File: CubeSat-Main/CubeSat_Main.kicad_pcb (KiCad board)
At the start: 2 copper layers, 92 x 92 mm, 25 parts, among them J1 Conn_01x03_Pin, J2 Conn_01x08_Socket, U1 STM32F411CEU6 - BlackPill, U2 LORA E220-900T22D, U3 BNO055, U4 GPS_NEO6M, U6 LM35-LP

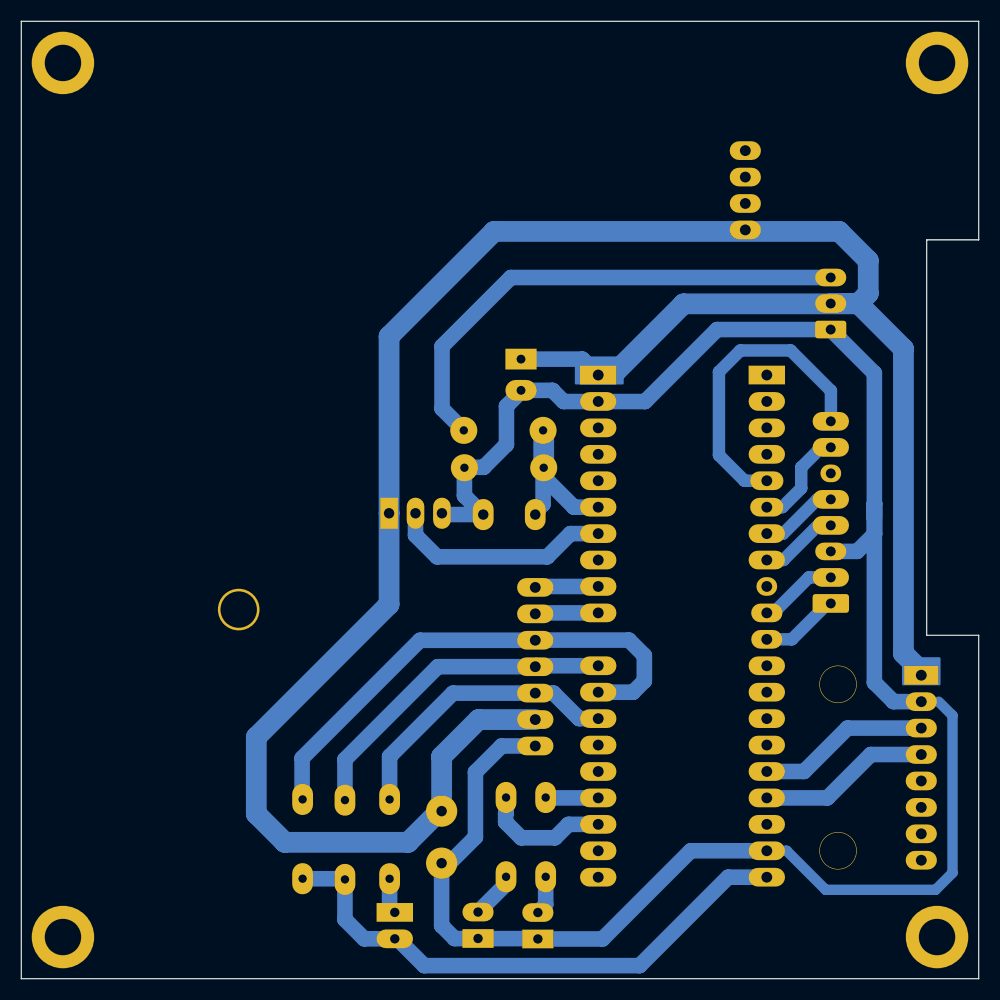
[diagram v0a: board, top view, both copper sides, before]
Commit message: adding the unused pin as smd, instead of just removing it
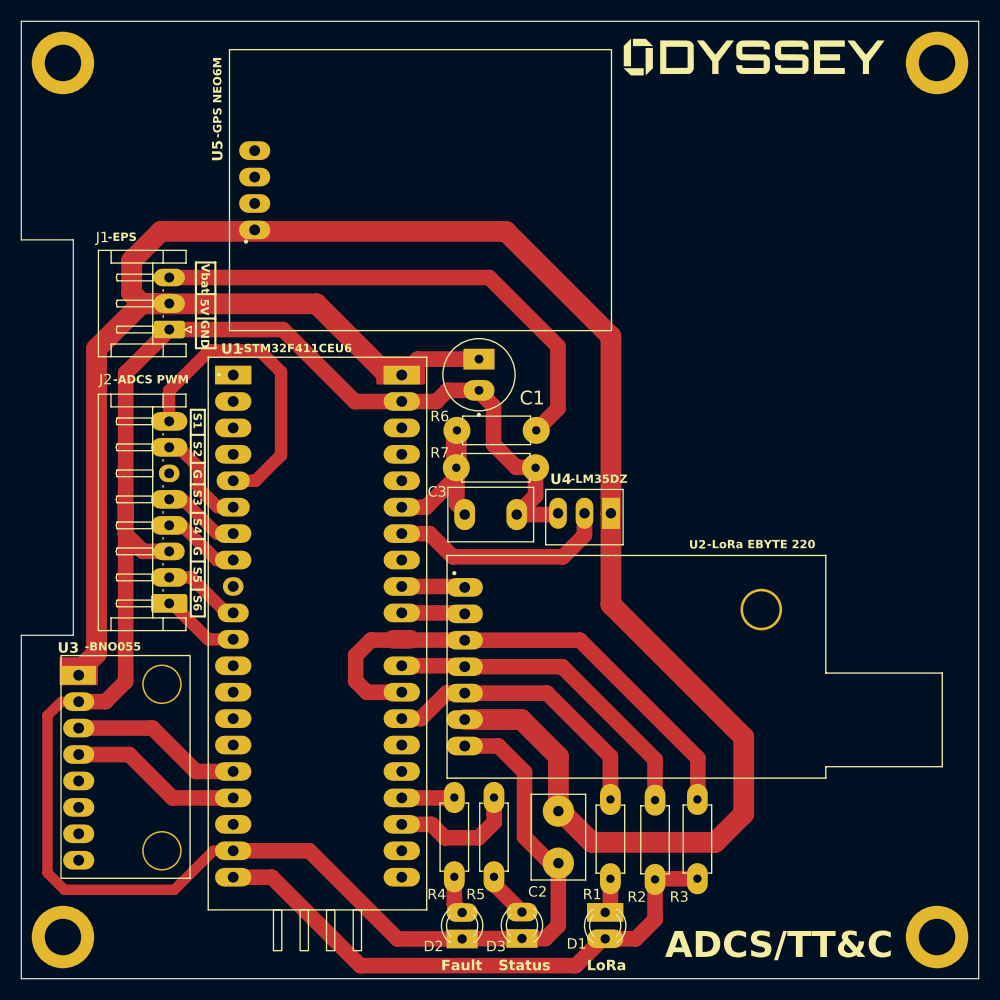
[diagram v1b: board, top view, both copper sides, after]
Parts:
- C1, C2, C3, D1, D2, D3, G***, J1, J2, R1, R2, R3, R4, R5, R6, R7, REF** (x4), U1, U2, U3: moved to F.Cu
- U4: renamed from U6; moved to F.Cu
- U5: renamed from U4; moved to F.Cu
- moved REF** 84.0 mm to (88.0, -4.00), turned to 0 degrees
- moved REF** 84.0 mm to (4.00, -4.00), turned to 0 degrees
- moved REF** 84.0 mm to (88.0, -88.0), turned to 0 degrees
- moved REF** 84.0 mm to (4.00, -88.0), turned to 0 degrees
- moved U3 72.0 mm to (10.0, -20.3), turned to 180 degrees
- moved J2 63.6 mm to (14.2, -36.1)
- moved J1 63.6 mm to (14.2, -62.4)
- moved G*** 49.0 mm to (70.5, -88.6), turned to 0 degrees
- moved R3 37.9 mm to (65.0, -17.2)
- moved U1 35.1 mm to (28.5, -33.5), turned to 0 degrees
- moved R2 29.8 mm to (60.9, -17.2)
- moved U2 26.2 mm to (59.1, -30.0)
- moved R1 21.2 mm to (56.6, -17.2)
- moved D1 20.2 mm to (56.1, -6.37)
- moved U4 16.2 mm to (54.1, -44.7)
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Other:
- outline, holes or cut-outs redrawn

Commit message: change in the GPS location, so it doesnt smash into its antenna
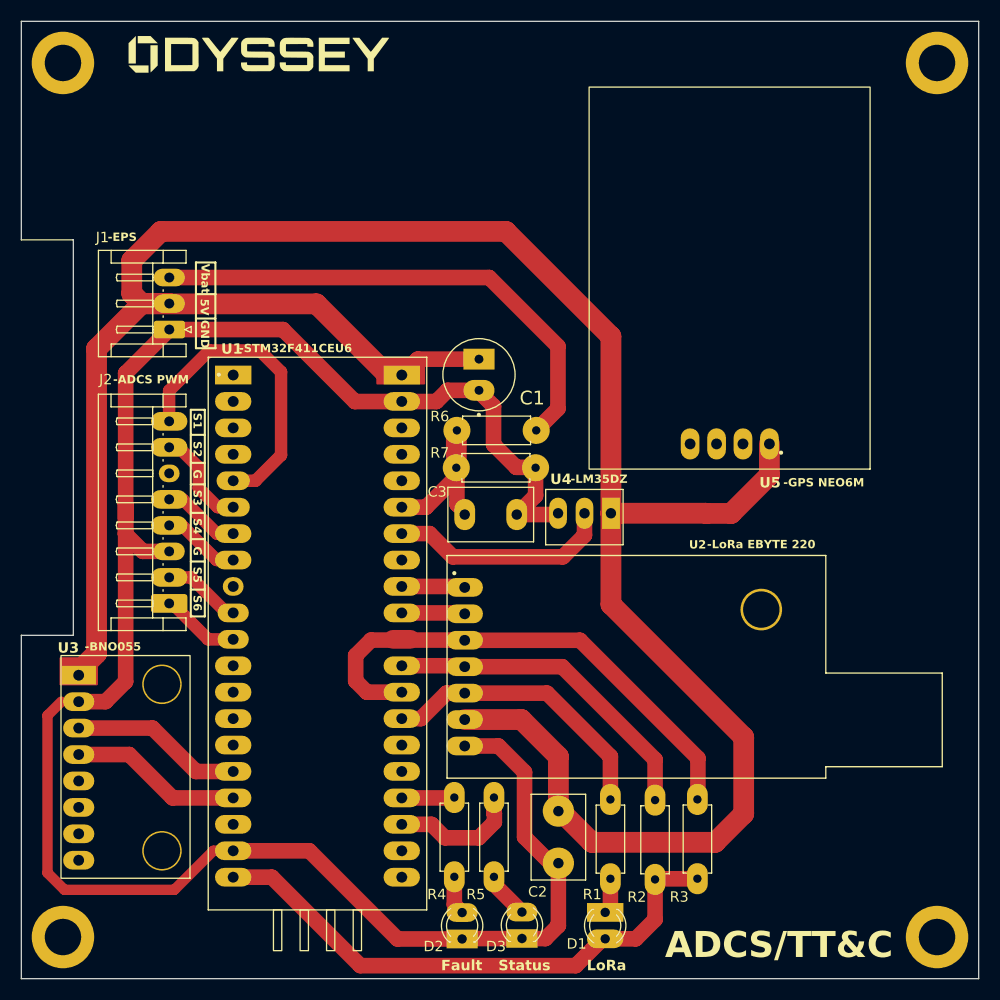
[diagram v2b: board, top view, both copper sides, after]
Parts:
- moved G*** 47.6 mm to (22.9, -88.8)
- moved U5 31.4 mm to (68.0, -66.9), turned to 180 degrees
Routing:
- net VIN_5V: track 219.1 -> 238.9 mm
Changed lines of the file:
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@@
 	(footprint "Cubesat_Modules:GPS_NEO6M"
 		(layer "F.Cu")
-		(at 37.915 -75.895 90)
+		(at 67.95 -66.88 180)
 		(property "Reference" "U5"
-			(at 3.665 -19.055 90)
+			(at -4 -19.21 0)
 			(unlocked yes)
 			(layer "F.SilkS")
@@
 		)
 		(property "Value" "GPS_NEO6M"
-			(at 0 -1.5 90)
+			(at 0 -1.5 180)
 			(unlocked yes)
 			(layer "F.Fab")
@@
 		)
 		(property "Datasheet" ""
-			(at 0 0 90)
+			(at 0 0 180)
 			(unlocked yes)
 			(layer "F.Fab")
@@
 		)
 		(property "Description" ""
-			(at 0 0 90)
+			(at 0 0 180)
 			(unlocked yes)
 			(layer "F.Fab")
@@
 		)
 		(fp_text user "${REFERENCE}"
-			(at 0 0 90)
+			(at 0 0 180)
 			(unlocked yes)
 			(layer "F.Fab")
@@
 		)
 		(pad "1" thru_hole oval
-			(at -3.94 -15.49 180)
+			(at -3.94 -15.49 270)
 			(size 3 1.8)
 			(drill 1.04)
@@
 		)
 		(pad "2" thru_hole oval
-			(at -1.4 -15.49 180)
+			(at -1.4 -15.49 270)
 			(size 3 1.8)
 			(drill 1.04)
@@
 		)
 		(pad "3" thru_hole oval
-			(at 1.14 -15.49 180)
+			(at 1.14 -15.49 270)
 			(size 3 1.8)
 			(drill 1.04)
@@
 		)
 		(pad "4" thru_hole oval
-			(at 3.68 -15.49 180)
+			(at 3.68 -15.49 270)
 			(size 3 1.8)
 			(drill 1.04)
@@
 		)
 		(property "Value" "Conn_01x03_Pin"
-			(at 19.3375 -0.350002 90)
+			(at 11.49 -1.66 0)
 			(layer "F.Fab")
 			(effects
@@
 	(footprint "Logos:Odyssey_Logo_2"
 		(layer "F.Cu")
-		(at 70.49 -88.56)
+		(at 22.901622 -88.824623)
 		(property "Reference" "G***"
 			(at 4.318378 10.074623 0)
@@
 	)
 	(gr_text "-GPS NEO6M"
-		(at 19.32 -80.79 90)
+		(at 73.22 -47.21 0)
 		(layer "F.SilkS")
 		(effects
@@
 	)
 	(segment
+		(start 65.805 -44.725)
+		(end 65.82 -44.71)
+		(width 2)
+		(layer "F.Cu")
+		(net 1)
+	)
+	(segment
 		(start 46.57 -71.81)
 		(end 13.41 -71.81)
@@
 	)
 	(segment
+		(start 68.22 -44.71)
+		(end 71.89 -48.38)
+		(width 2)
+		(layer "F.Cu")
+		(net 1)
+	)
+	(segment
 		(start 51.61 -21.35)
 		(end 48.06 -24.9)
@@
 	)
 	(segment
+		(start 65.82 -44.71)
+		(end 68.22 -44.71)
+		(width 2)
+		(layer "F.Cu")
+		(net 1)
+	)
+	(segment
 		(start 34.9225 -58.2875)
 		(end 36.46 -58.2875)
@@
 		(width 2)
 		(layer "F.Cu")
+		(net 1)
+	)
+	(segment
+		(start 71.89 -48.38)
+		(end 71.89 -51.39)
+		(width 2)
+		(layer "F.Cu")
+		(net 1)
+	)
+	(segment
+		(start 56.66 -44.725)
+		(end 65.805 -44.725)
+		(width 2)
+		(layer "F.Cu")

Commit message: small changes only
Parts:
- C1, C2, C3, D1, D2, D3, G***, J1, J2, R1, R2, R3, R4, R5, R6, R7, REF** (x4), U1, U2, U3, U4, U5: moved to B.Cu
- moved REF** 84.0 mm to (4.00, -4.00), turned to 180 degrees
- moved REF** 84.0 mm to (88.0, -4.00), turned to 180 degrees
- moved REF** 84.0 mm to (4.00, -88.0), turned to 180 degrees
- moved REF** 84.0 mm to (88.0, -88.0), turned to 180 degrees
- moved U3 72.0 mm to (82.0, -20.3), turned to 0 degrees
- moved J2 63.6 mm to (77.8, -36.1)
- moved J1 63.6 mm to (77.8, -62.4)
- moved G*** 46.2 mm to (69.1, -88.8), turned to 180 degrees
- moved U5 43.9 mm to (24.1, -66.9), turned to 0 degrees
- moved R3 37.9 mm to (27.0, -17.2)
- moved U1 35.1 mm to (63.5, -33.5), turned to 180 degrees
- moved R2 29.8 mm to (31.1, -17.2)
- moved U2 26.2 mm to (32.9, -30.0)
- moved R1 21.2 mm to (35.4, -17.2)
- moved D1 20.2 mm to (35.9, -6.37)
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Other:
- outline, holes or cut-outs redrawn

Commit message: small changes in layout
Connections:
- U1 pad 26: unconnected-(U1-PB13-Pad26) -> M1_PWM1
- U1 pad 27: unconnected-(U1-PB14-Pad27) -> M1_PWM2
- U1 pad 29: M1_PWM1 -> unconnected-(U1-PA8-Pad29)
- U1 pad 30: M1_PWM2 -> unconnected-(U1-PA9-Pad30)
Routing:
- net M1_PWM1: track 30.4 -> 7.00 mm
- net M1_PWM2: track 9.70 -> 6.92 mm
- net unconnected-(U1-PA8-Pad29): track 0.00 -> 0.51 mm
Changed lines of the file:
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@@
 	(net 41 "unconnected-(U1-5V-Pad5V2)")
 	(net 42 "unconnected-(U3-ADO-Pad5)")
-	(net 43 "unconnected-(U1-PB14-Pad27)")
-	(net 44 "unconnected-(U1-PB13-Pad26)")
+	(net 43 "unconnected-(U1-PA9-Pad30)")
+	(net 44 "unconnected-(U1-PA8-Pad29)")
 	(net 45 "unconnected-(U5-TX-Pad3)")
 	(net 46 "unconnected-(U5-GND-Pad4)")
@@
 			(layers "*.Cu" "*.Mask")
 			(remove_unused_layers no)
-			(net 44 "unconnected-(U1-PB13-Pad26)")
+			(net 4 "M1_PWM1")
 			(pinfunction "PB13")
-			(pintype "bidirectional+no_connect")
+			(pintype "bidirectional")
 			(solder_mask_margin 0.102)
 		)
@@
 			(layers "*.Cu" "*.Mask")
 			(remove_unused_layers no)
-			(net 43 "unconnected-(U1-PB14-Pad27)")
+			(net 17 "M1_PWM2")
 			(pinfunction "PB14")
-			(pintype "bidirectional+no_connect")
+			(pintype "bidirectional")
 			(solder_mask_margin 0.102)
 		)
@@
 			(layers "*.Cu" "*.Mask")
 			(remove_unused_layers no)
-			(net 4 "M1_PWM1")
+			(net 44 "unconnected-(U1-PA8-Pad29)")
 			(pinfunction "PA8")
-			(pintype "bidirectional")
+			(pintype "bidirectional+no_connect")
 			(solder_mask_margin 0.102)
 		)
@@
 			(layers "*.Cu" "*.Mask")
 			(remove_unused_layers no)
-			(net 17 "M1_PWM2")
+			(net 43 "unconnected-(U1-PA9-Pad30)")
 			(pinfunction "PA9")
-			(pintype "bidirectional")
+			(pintype "bidirectional+no_connect")
 			(solder_mask_margin 0.102)
 		)
@@
 		(pad "33" thru_hole oval
 			(at -8.1 4.18 180)
-			(size 2 1.8)
+			(size 1.8 1.8)
 			(drill 1.04)
 			(layers "*.Cu" "*.Mask")
@@
 		(pad "6" thru_hole oval
 			(at 12.5 0 90)
-			(size 1.7 2)
+			(size 1.8 3.5)
 			(drill 0.95)
 			(layers "*.Cu" "*.Mask")
@@
 	)
 	(gr_rect
-		(start 75.715 -54.67)
-		(end 74.365 -34.81)
+		(start 74.365 -54.67)
+		(end 75.715 -34.81)
 		(stroke
 			(width 0.2)
@@
 	)
 	(gr_rect
-		(start 75.22 -68.825)
-		(end 73.35 -60.585)
+		(start 73.35 -68.825)
+		(end 75.22 -60.585)
 		(stroke
 			(width 0.2)
@@
 	)
 	(segment
-		(start 67.04 -50.31)
-		(end 69.5 -47.85)
-		(width 1.2)
-		(layer "B.Cu")
-		(net 4)
-	)
-	(segment
-		(start 77.8 -56.5)
-		(end 73.93 -60.37)
-		(width 1.2)
-		(layer "B.Cu")
-		(net 4)
-	)
-	(segment
-		(start 67.04 -58.31)
-		(end 67.04 -50.31)
-		(width 1.2)
-		(layer "B.Cu")
-		(net 4)
-	)
-	(segment
-		(start 69.5 -47.85)
-		(end 71.64 -47.85)
-		(width 1.2)
-		(layer "B.Cu")
-		(net 4)
-	)
-	(segment
-		(start 77.79 -53.56)
-		(end 77.8 -53.57)
-		(width 1.2)
-		(layer "B.Cu")
-		(net 4)
-	)
-	(segment
-		(start 71.64 -47.949939)
-		(end 71.64 -47.95)
-		(width 0.2)
-		(layer "B.Cu")
-		(net 4)
-	)
-	(segment
-		(start 71.6575 -47.932439)
-		(end 71.64 -47.949939)
-		(width 0.2)
+		(start 75.88 -55.47)
+		(end 71.64 -55.47)
+		(width 1.5)
 		(layer "B.Cu")
 		(net 4)
@@
 	)
 	(segment
-		(start 77.8 -53.57)
-		(end 77.8 -56.5)
-		(width 1.2)
-		(layer "B.Cu")
-		(net 4)
-	)
-	(segment
-		(start 69.1 -60.37)
-		(end 67.04 -58.31)
-		(width 1.2)
-		(layer "B.Cu")
-		(net 4)
-	)
-	(segment
-		(start 71.64 -47.85)
-		(end 72.13 -47.85)
-		(width 1)
+		(start 77.79 -53.56)
+		(end 75.88 -55.47)
+		(width 1.5)
 		(layer "B.Cu")
 		(net 4)
 	)
 	(segment
-		(start 73.93 -60.37)
-		(end 69.1 -60.37)
+		(start 76.25 -46.06)
+		(end 77.79 -46.06)
 		(width 1.2)
 		(layer "B.Cu")
-		(net 4)
+		(net 7)
 	)
 	(segment
@@
 	)
 	(segment
-		(start 76.5 -46.06)
-		(end 77.79 -46.06)
+		(start 71.64 -42.77)
+		(end 72.96 -42.77)
 		(width 1.2)
 		(layer "B.Cu")
@@
 	)
 	(segment
-		(start 71.707561 -42.83)
-		(end 71.73 -42.852439)
-		(width 0.2)
-		(layer "B.Cu")
-		(net 7)
-	)
-	(segment
-		(start 71.64 -42.77)
-		(end 73.21 -42.77)
+		(start 72.96 -42.77)
+		(end 76.25 -46.06)
 		(width 1.2)
 		(layer "B.Cu")
@@
 	)
 	(segment
-		(start 73.21 -42.77)
-		(end 76.5 -46.06)
-		(width 1.2)
+		(start 71.707561 -42.83)
+		(end 71.73 -42.852439)
+		(width 0.2)
 		(layer "B.Cu")
 		(net 7)
@@
 		(start 74.05 -32.61)
 		(end 71.64 -32.61)
-		(width 1.2)
+		(width 1.5)
 		(layer "B.Cu")
 		(net 12)
@@
 		(start 77.79 -36.06)
 		(end 77.5 -36.06)
-		(width 1.2)
+		(width 1.5)
 		(layer "B.Cu")
 		(net 12)
@@
 		(start 77.5 -36.06)
 		(end 74.05 -32.61)
-		(width 1.2)
+		(width 1.5)
 		(layer "B.Cu")
 		(net 12)
@@
 	)
 	(segment
-		(start 72.27 -35.15)
+		(start 72.37 -35.15)
 		(end 71.64 -35.15)
-		(width 1.2)
+		(width 1.5)
 		(layer "B.Cu")
 		(net 16)
 	)
 	(segment
-		(start 75.68 -38.56)
-		(end 72.27 -35.15)
-		(width 1.2)
+		(start 75.78 -38.56)
+		(end 72.37 -35.15)
+		(width 1.5)
 		(layer "B.Cu")
 		(net 16)
@@
 	(segment
 		(start 77.79 -38.56)
-		(end 75.68 -38.56)
-		(width 1.2)
+		(end 75.78 -38.56)
+		(width 1.5)
 		(layer "B.Cu")
 		(net 16)
 	)
 	(segment
-		(start 74.95 -49.13)
-		(end 76.88 -51.06)
-		(width 1.2)
+		(start 73.44 -52.93)
+		(end 75.31 -51.06)
+		(width 1.5)
 		(layer "B.Cu")
 		(net 17)
 	)
 	(segment
-		(start 76.88 -51.06)
+		(start 75.31 -51.06)
 		(end 77.79 -51.06)
-		(width 1.2)
-		(layer "B.Cu")
-		(net 17)
-	)
-	(segment
-		(start 74.95 -47.13)
-		(end 74.95 -49.13)
-		(width 1.2)
-		(layer "B.Cu")
-		(net 17)
-	)
-	(segment
-		(start 73.13 -45.31)
-		(end 74.95 -47.13)
-		(width 1.2)
+		(width 1.5)
 		(layer "B.Cu")
 		(net 17)
 	)
 	(segment
-		(start 71.64 -45.31)
-		(end 73.13 -45.31)
-		(width 1.2)
+		(start 71.64 -52.93)
+		(end 73.44 -52.93)
+		(width 1.5)
 		(layer "B.Cu")
 		(net 17)
@@
 	)
 	(segment
+		(start 71.64 -47.949939)
+		(end 71.64 -47.95)
+		(width 0.2)
+		(layer "B.Cu")
+		(net 44)
+	)
+	(segment
+		(start 71.6575 -47.932439)
+		(end 71.64 -47.949939)
+		(width 0.2)
+		(layer "B.Cu")
+		(net 44)
+	)
+	(segment
+		(start 71.64 -47.85)
+		(end 72.13 -47.85)
+		(width 1)
+		(layer "B.Cu")
+		(net 44)
+	)
+	(segment

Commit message: minor changes in the design
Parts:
- C1, C2, C3, D1, D2, D3, G***, J1, J2, R1, R2, R3, R4, R5, R6, R7, REF** (x4), U1, U2, U3, U4, U5: moved to F.Cu
- moved REF** 84.0 mm to (88.0, -4.00), turned to 0 degrees
- moved REF** 84.0 mm to (4.00, -4.00), turned to 0 degrees
- moved REF** 84.0 mm to (88.0, -88.0), turned to 0 degrees
- moved REF** 84.0 mm to (4.00, -88.0), turned to 0 degrees
- moved U3 72.0 mm to (10.0, -20.3), turned to 180 degrees
- moved J2 63.6 mm to (14.2, -36.1)
- moved J1 63.6 mm to (14.2, -62.4)
- moved G*** 46.2 mm to (22.9, -88.8), turned to 0 degrees
- moved U5 43.9 mm to (68.0, -66.9), turned to 180 degrees
- moved R3 37.9 mm to (65.0, -17.2)
- moved U1 35.1 mm to (28.5, -33.5), turned to 0 degrees
- moved R2 29.8 mm to (60.9, -17.2)
- moved U2 26.2 mm to (59.1, -30.0)
- moved R1 21.2 mm to (56.6, -17.2)
- moved D1 20.2 mm to (56.1, -6.37)
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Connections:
- R4 pad 1: LED_RED -> LED_BLUE
- R5 pad 1: LED_BLUE -> LED_RED
- U1 pad 3: LED_BLUE -> LED_RED
- U1 pad 4: LED_RED -> LED_BLUE
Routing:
- net LED_RED: track 5.65 -> 12.4 mm
- net LED_BLUE: track 12.4 -> 5.65 mm
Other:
- outline, holes or cut-outs redrawn
